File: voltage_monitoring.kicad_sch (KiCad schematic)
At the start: 8 parts

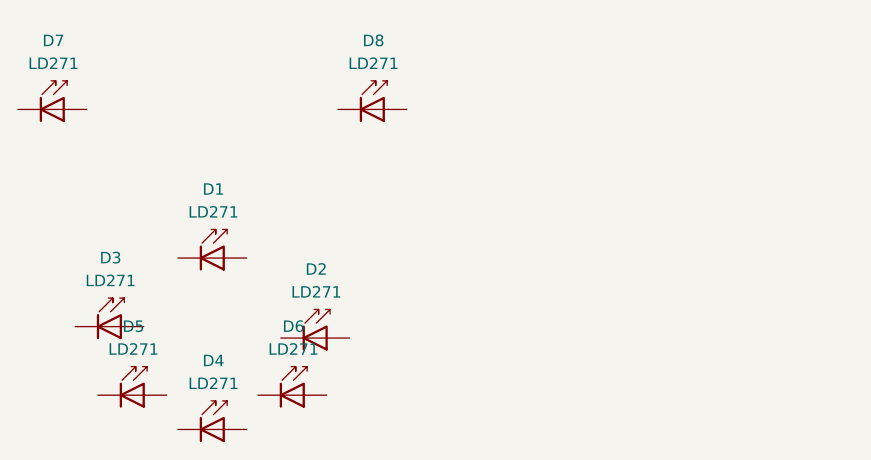
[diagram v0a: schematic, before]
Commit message: voltage monitoring schematic done
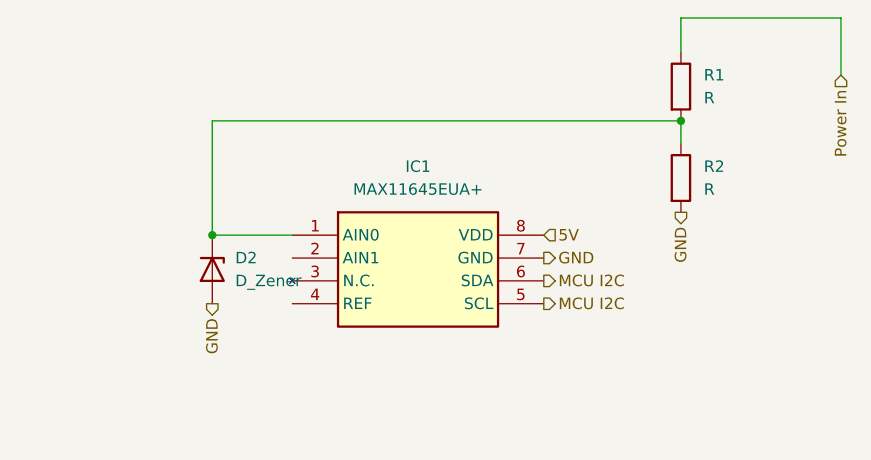
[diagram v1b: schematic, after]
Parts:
- removed D1, D2, D3, D4, D5, D6, D7, D8: LD271, LED_THT:LED_D5.0mm_IRGrey, symbol LED:LD271
- added D2: D_Zener, symbol Device:D_Zener
- added IC1: MAX11645EUA+, SOP65P490X111-8N, symbol MAX11645EUA+:MAX11645EUA+
- added R1, R2: R, symbol Device:R
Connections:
- new net: D2.1 (K), IC1.1 (AIN0), R1.2, R2.1
- new net 5V: IC1.8 (VDD)
- new net GND: D2.2 (A), IC1.7 (GND), R2.2
- new net MCU I2C: IC1.5 (SCL), IC1.6 (SDA)
- new net Power In: R1.1
